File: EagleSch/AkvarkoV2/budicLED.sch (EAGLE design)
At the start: 83 parts, among them IC1 7805T, IC2 4051N, IC3 LF33CV, IC4 ESP01, J1 TRANSFLASH-LOCK, Q1 BD243C, Q2 BD243C, Q3 BD243C, Q4 BD243C, Q5 BC546A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

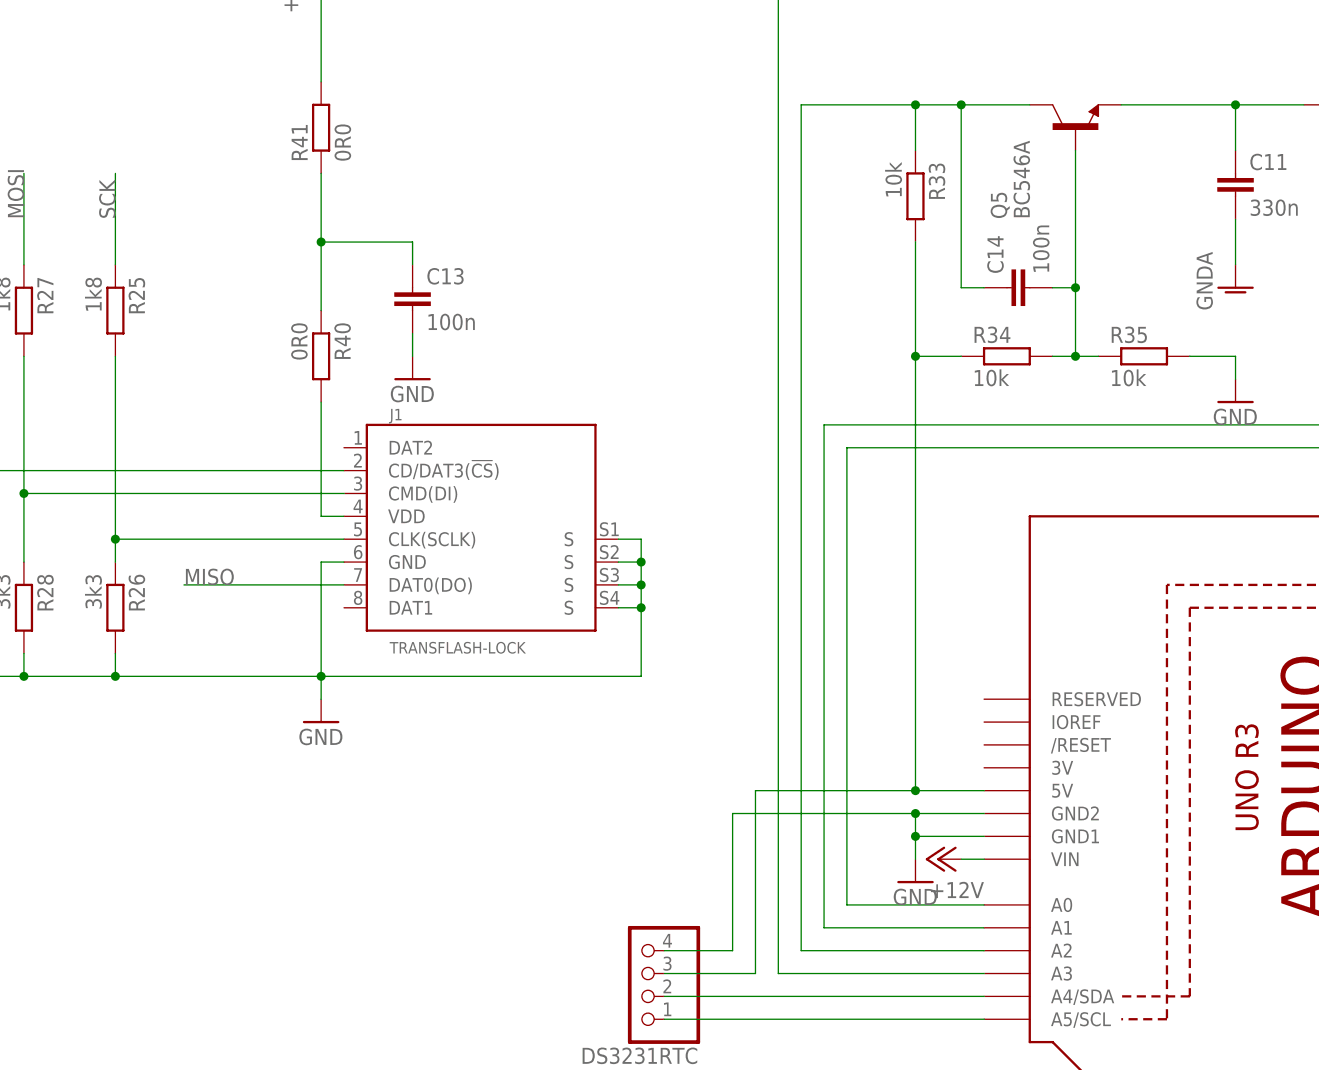
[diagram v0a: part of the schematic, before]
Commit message: - upraveny hodnoty odporu u zesilovace napeti z bocniku - pridana dioda do napajeciho vstupu ARDUINO
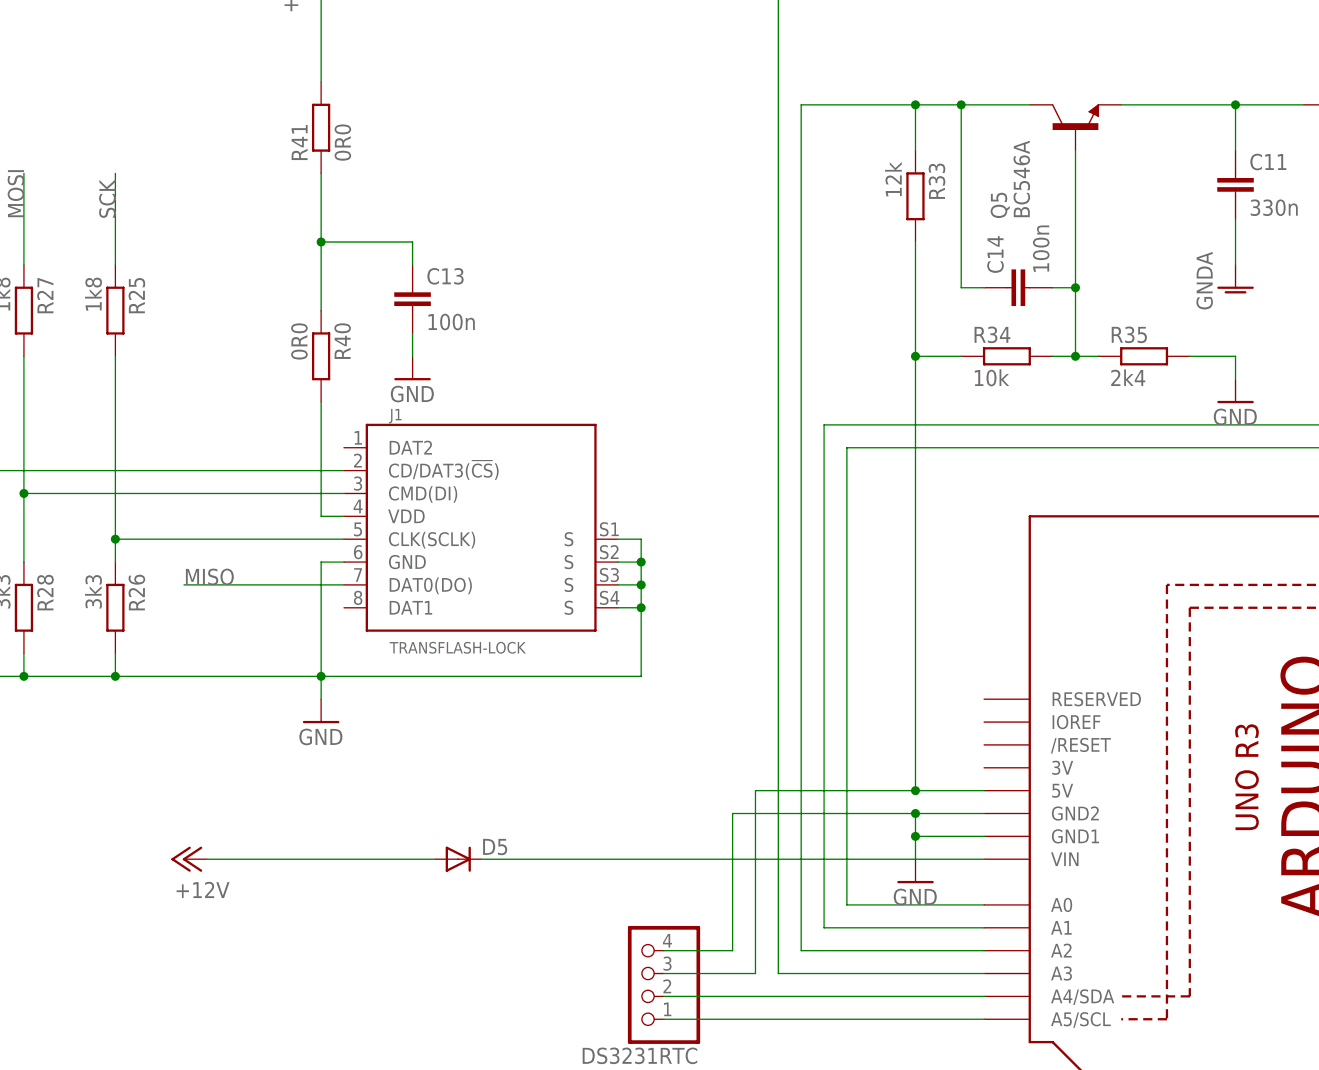
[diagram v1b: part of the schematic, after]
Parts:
- added D5: (no value), diode:DIODE-MELF-MLL41
- R33: value 10k -> 12k
- R35: value 10k -> 2k4
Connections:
- new net N$48: D5.C, U1.VIN
- net +12V: now also D5.A; no longer U1.VIN
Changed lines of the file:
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@@
 <part name="C13" library="rcl" deviceset="C-EU" device="C1206K" value="100n"/>
 <part name="Q5" library="transistor-npn" deviceset="BC546*" device="" technology="A"/>
-<part name="R33" library="rcl" deviceset="R-EU_" device="0207/12" value="10k"/>
+<part name="R33" library="rcl" deviceset="R-EU_" device="0207/12" value="12k"/>
 <part name="R34" library="rcl" deviceset="R-EU_" device="0207/12" value="10k"/>
-<part name="R35" library="rcl" deviceset="R-EU_" device="0207/12" value="10k"/>
+<part name="R35" library="rcl" deviceset="R-EU_" device="0207/12" value="2k4"/>
 <part name="C14" library="rcl" deviceset="C-EU" device="C1206K" value="100n"/>
 <part name="LED2" library="led" deviceset="LED" device="3MM" value="2.2V 25mA"/>
@@
 <part name="R41" library="rcl" deviceset="R-EU_" device="0207/12" value="0R0"/>
 <part name="GND26" library="supply1" deviceset="GND" device=""/>
+<part name="D5" library="diode" deviceset="DIODE-" device="MELF-MLL41"/>
 </parts>
 <sheets>
@@
 <instance part="IC2" gate="A" x="-55.88" y="111.76" rot="MR0"/>
 <instance part="IC2" gate="P" x="106.68" y="185.42" rot="R90"/>
-<instance part="P+3" gate="1" x="-109.22" y="43.18" rot="R90"/>
+<instance part="P+3" gate="1" x="-193.04" y="43.18" rot="R90"/>
 <instance part="C11" gate="G$1" x="-76.2" y="119.38"/>
 <instance part="R23" gate="G$1" x="-55.88" y="0" rot="R180"/>
@@
 <instance part="R41" gate="G$1" x="-177.8" y="124.46" rot="R90"/>
 <instance part="GND26" gate="1" x="-167.64" y="96.52"/>
+<instance part="D5" gate="G$1" x="-162.56" y="43.18"/>
 </instances>
 <busses>
@@
 <segment>
 <pinref part="P+3" gate="1" pin="+12V"/>
-<pinref part="U1" gate="G$1" pin="VIN"/>
-<wire x1="-106.68" y1="43.18" x2="-104.14" y2="43.18" width="0.1524" layer="91"/>
+<wire x1="-190.5" y1="43.18" x2="-165.1" y2="43.18" width="0.1524" layer="91"/>
+<pinref part="D5" gate="G$1" pin="A"/>
 </segment>
 </net>
@@
 </segment>
 </net>
+<net name="N$48" class="0">
+<segment>
+<pinref part="U1" gate="G$1" pin="VIN"/>
+<pinref part="D5" gate="G$1" pin="C"/>
+<wire x1="-160.02" y1="43.18" x2="-104.14" y2="43.18" width="0.1524" layer="91"/>
+</segment>
+</net>
